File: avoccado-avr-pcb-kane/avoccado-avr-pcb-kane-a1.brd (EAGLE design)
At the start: 17.5 x 21.3 mm, 37 parts, among them IC5 ATMEGA328P-20MU, Q1 16MHz

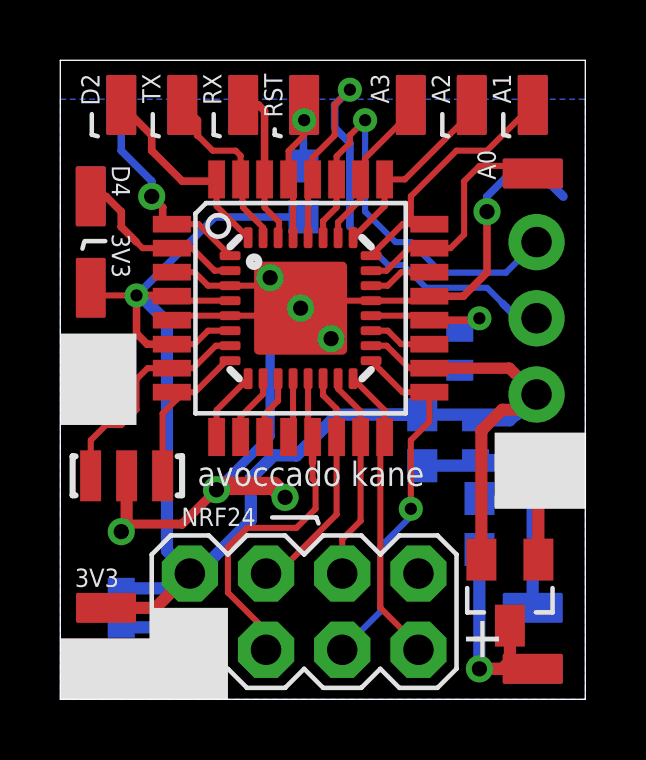
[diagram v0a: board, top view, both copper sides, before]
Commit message: start new 1 sq inch PCB fork 'yolandi'
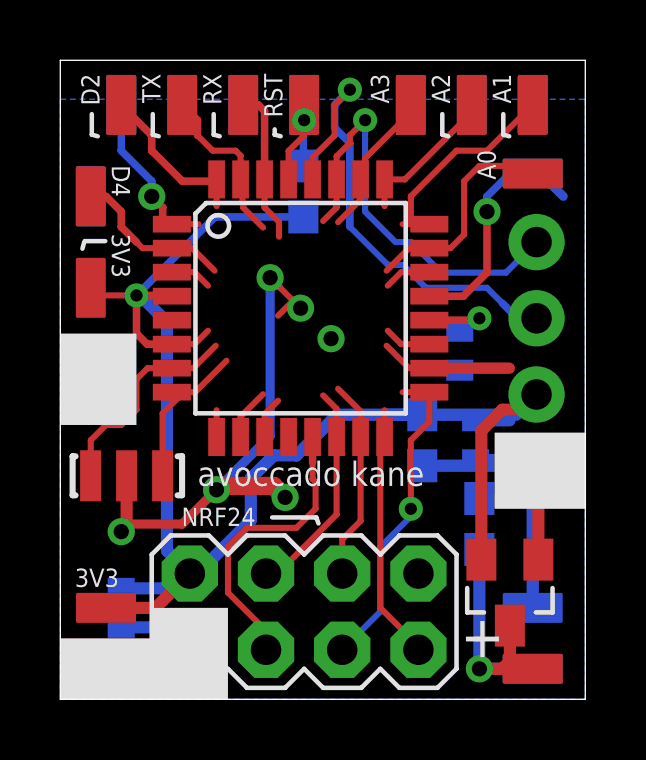
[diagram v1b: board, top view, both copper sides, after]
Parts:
- removed IC5: ATMEGA328P-20MU, idii:MLF32
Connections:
- net 3V3: now also MPU6050.1; no longer IC5.18, IC5.4, IC5.6, MPU6050.2
- net A0: no longer IC5.23
- net A1: no longer IC5.24
- net A2: no longer IC5.25
- net A3: no longer IC5.26
- net A4: no longer IC5.27
- net A5: no longer IC5.28
- net A6: no longer IC5.19
- net A7: no longer IC5.22
- net AREF: no longer IC5.20
- net D10: no longer IC5.14
- net D2: no longer IC5.32
- net D3: no longer IC5.1
- net D4: no longer IC5.2
- net D5: no longer IC5.9
- net D6: no longer IC5.10
- net D7: no longer IC5.11
- net D8: no longer IC5.12
- net D9: no longer IC5.13
- net GND: now also MPU6050.2; no longer IC5.21, IC5.3, IC5.5, MPU6050.1
- net MISO: no longer IC5.16
- net MOSI: no longer IC5.15
- net N$1: no longer IC5.8
- net N$2: no longer IC5.7
- net RESET: no longer IC5.29
- net RXI: no longer IC5.30
- net SCK: no longer IC5.17
- net TXO: no longer IC5.31
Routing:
- net GND: track 60.1 -> 48.8 mm
- net 3V3: track 63.6 -> 56.3 mm
- net D9: track 12.9 -> 11.1 mm
- net D8: track 2.00 -> 0.21 mm
- net AREF: track 4.53 -> 2.74 mm
- net RESET: track 6.75 -> 4.95 mm
- net A5: track 18.0 -> 16.2 mm
- net D5: track 2.38 -> 0.89 mm
- net SCK: track 12.2 -> 10.7 mm
- net MISO: track 10.1 -> 8.59 mm
- net D2: track 6.93 -> 5.44 mm
- net D3: track 7.23 -> 5.74 mm
- net A2: track 6.46 -> 4.98 mm
- net A1: track 9.12 -> 7.63 mm
- net D7: track 2.13 -> 1.39 mm
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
